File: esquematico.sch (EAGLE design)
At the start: 15 parts, among them IC1 TS321IDBVR, IC2 ESP32-S3-WROOM-1-N16R8, IC3 MAX30102EFD+T

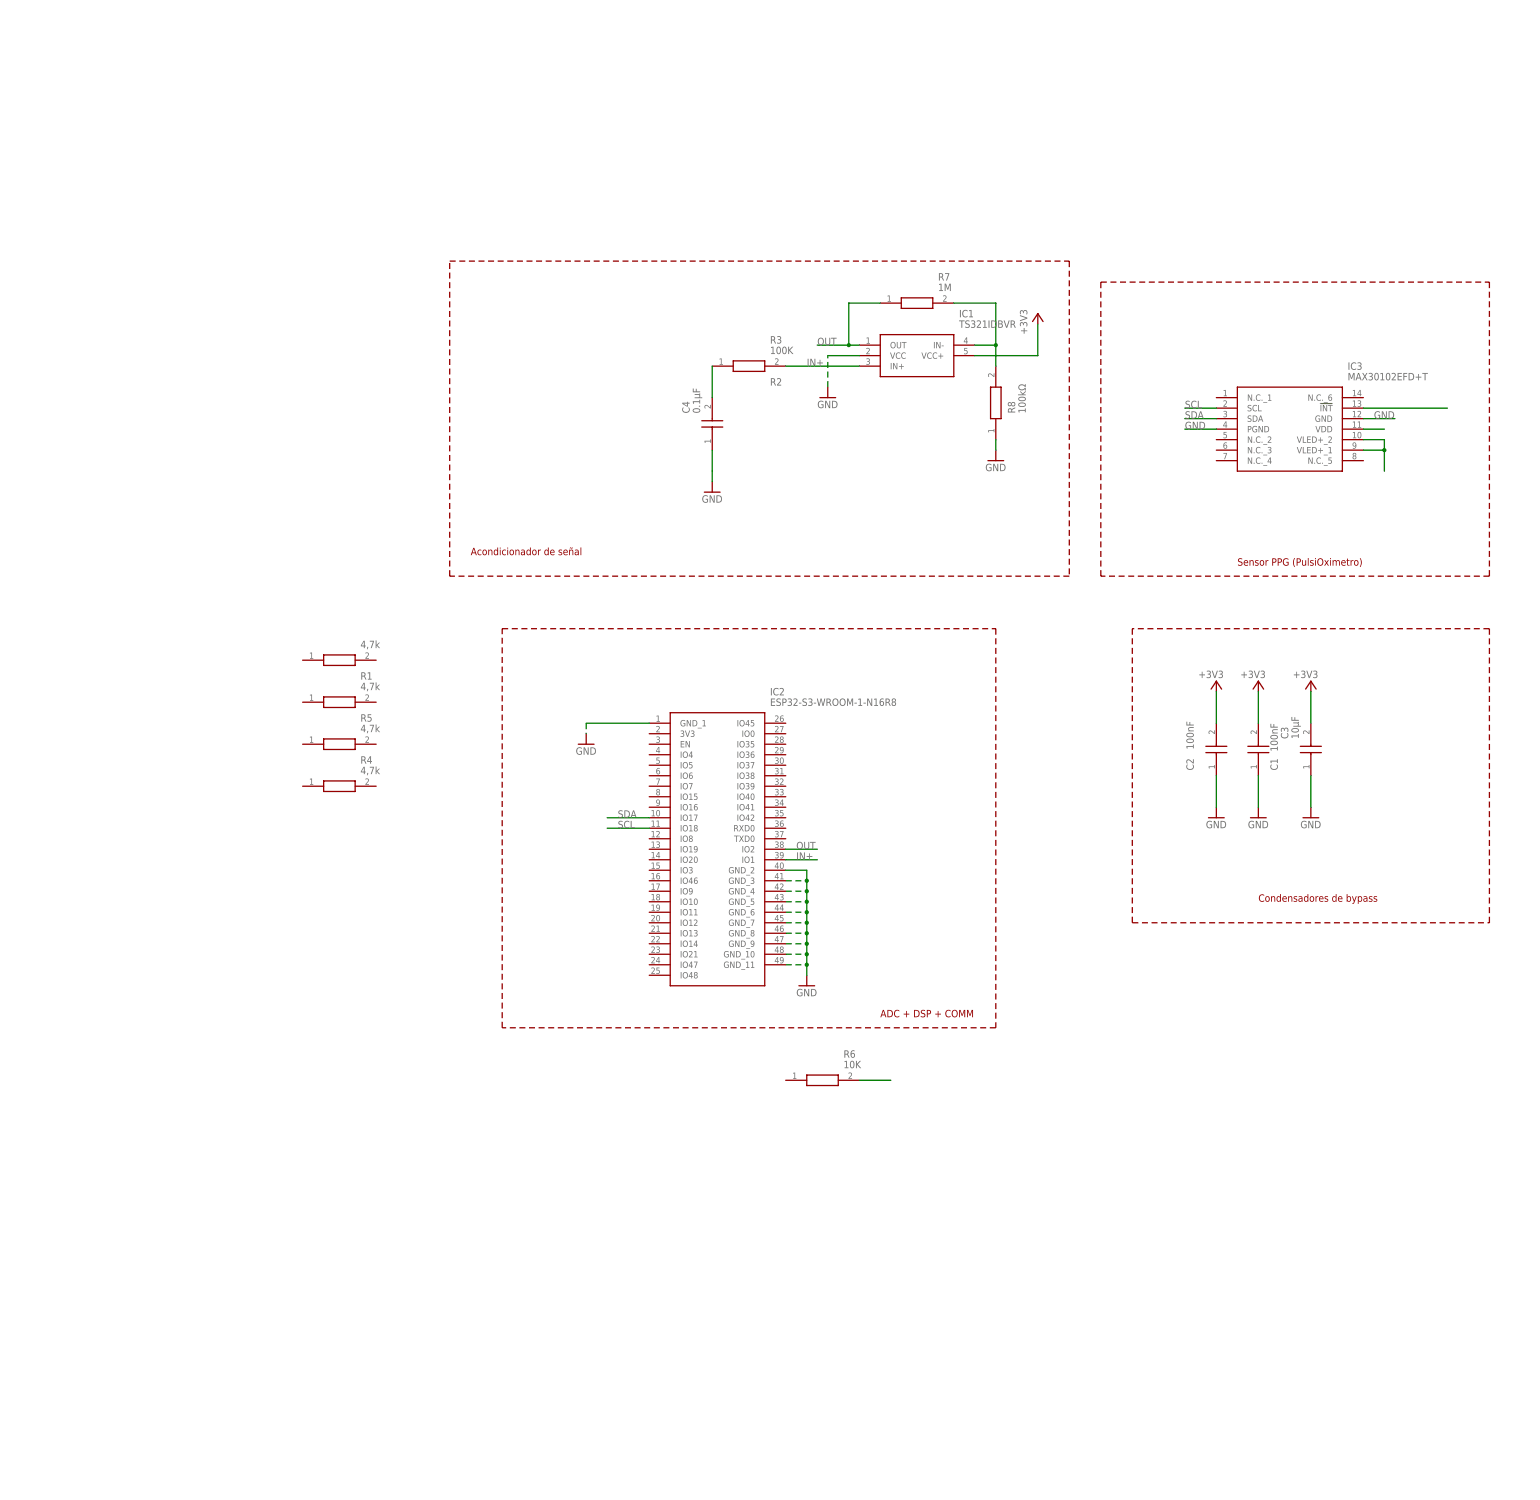
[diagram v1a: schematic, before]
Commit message: Finalizado bloque 2: Sensor PPG (PulsiOximetro)
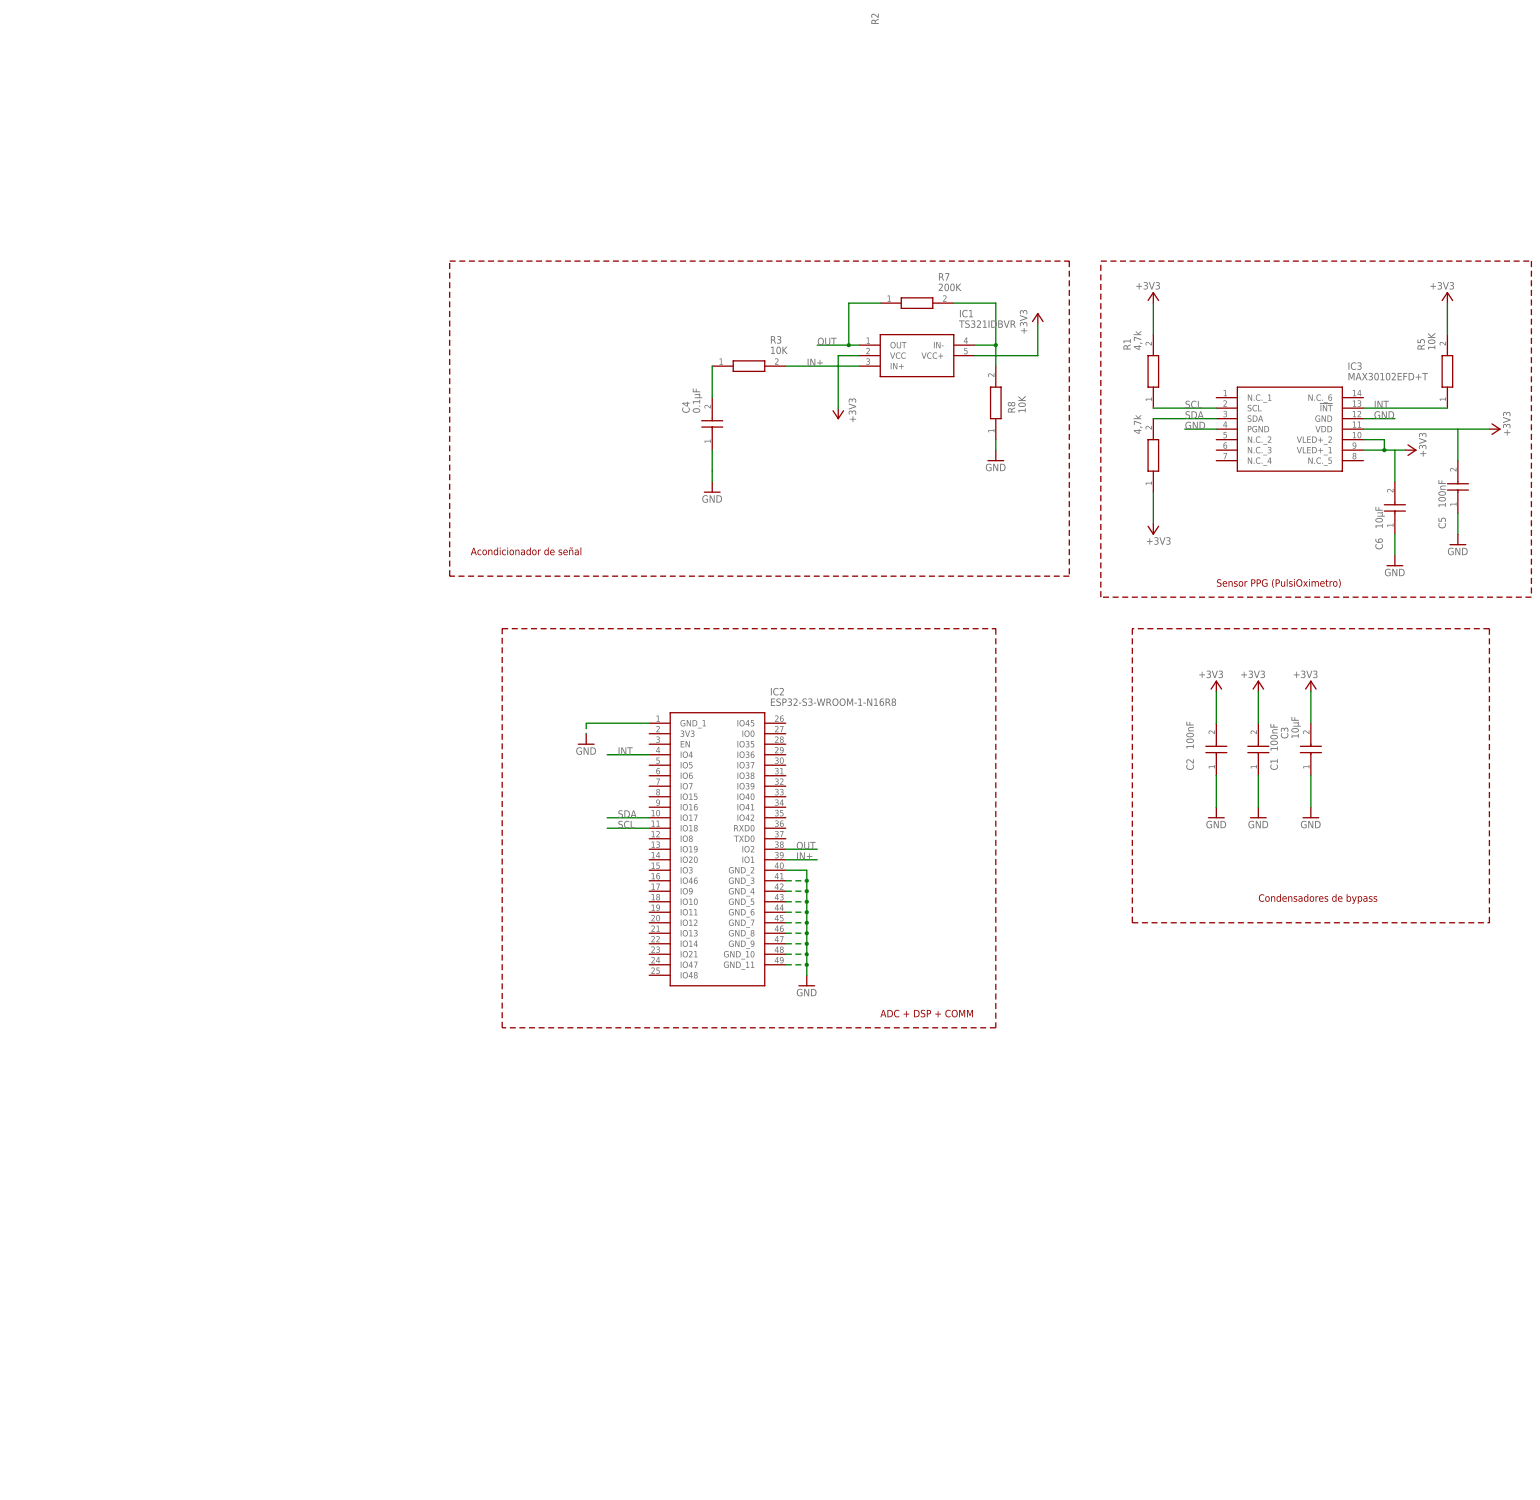
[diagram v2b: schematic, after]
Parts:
- removed R4: 4,7k, 0805S8F1202P5E:0805S8F1202P5E
- removed R6: 10K, 0805S8F1202P5E:0805S8F1202P5E
- added C5: 100nF, C0805J104K1RACAUTO:C0805J104K1RACAUTO
- added C6: 10µF, C0805J104K1RACAUTO:C0805J104K1RACAUTO
- R3: value 100K -> 10K
- R5: value 4,7k -> 10K
- R7: value 1M -> 200K
- R8: value 100kΩ -> 10K
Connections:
- removed net N$10: IC3.VDD
- removed net N$13: R6.2
- removed net N$15: IC3.!INT
- removed net N$16: IC3.VLED+_1, IC3.VLED+_2
- new net +3V1: C5.2
- new net +3V2: C6.2
- new net INT: IC2.IO4, IC3.!INT, R5.1
- net +3V3: now also IC1.VCC, IC3.VDD, IC3.VLED+_1, IC3.VLED+_2, R1.2, R2.1, R5.2
- net GND: now also C5.1, C6.1; no longer IC1.VCC
- net SCL: now also R1.1
- net SDA: now also R2.2
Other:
- moved on the sheet: R1, R2, R5

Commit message: Se corrigieron algunos bloques y se anoto lo faltante
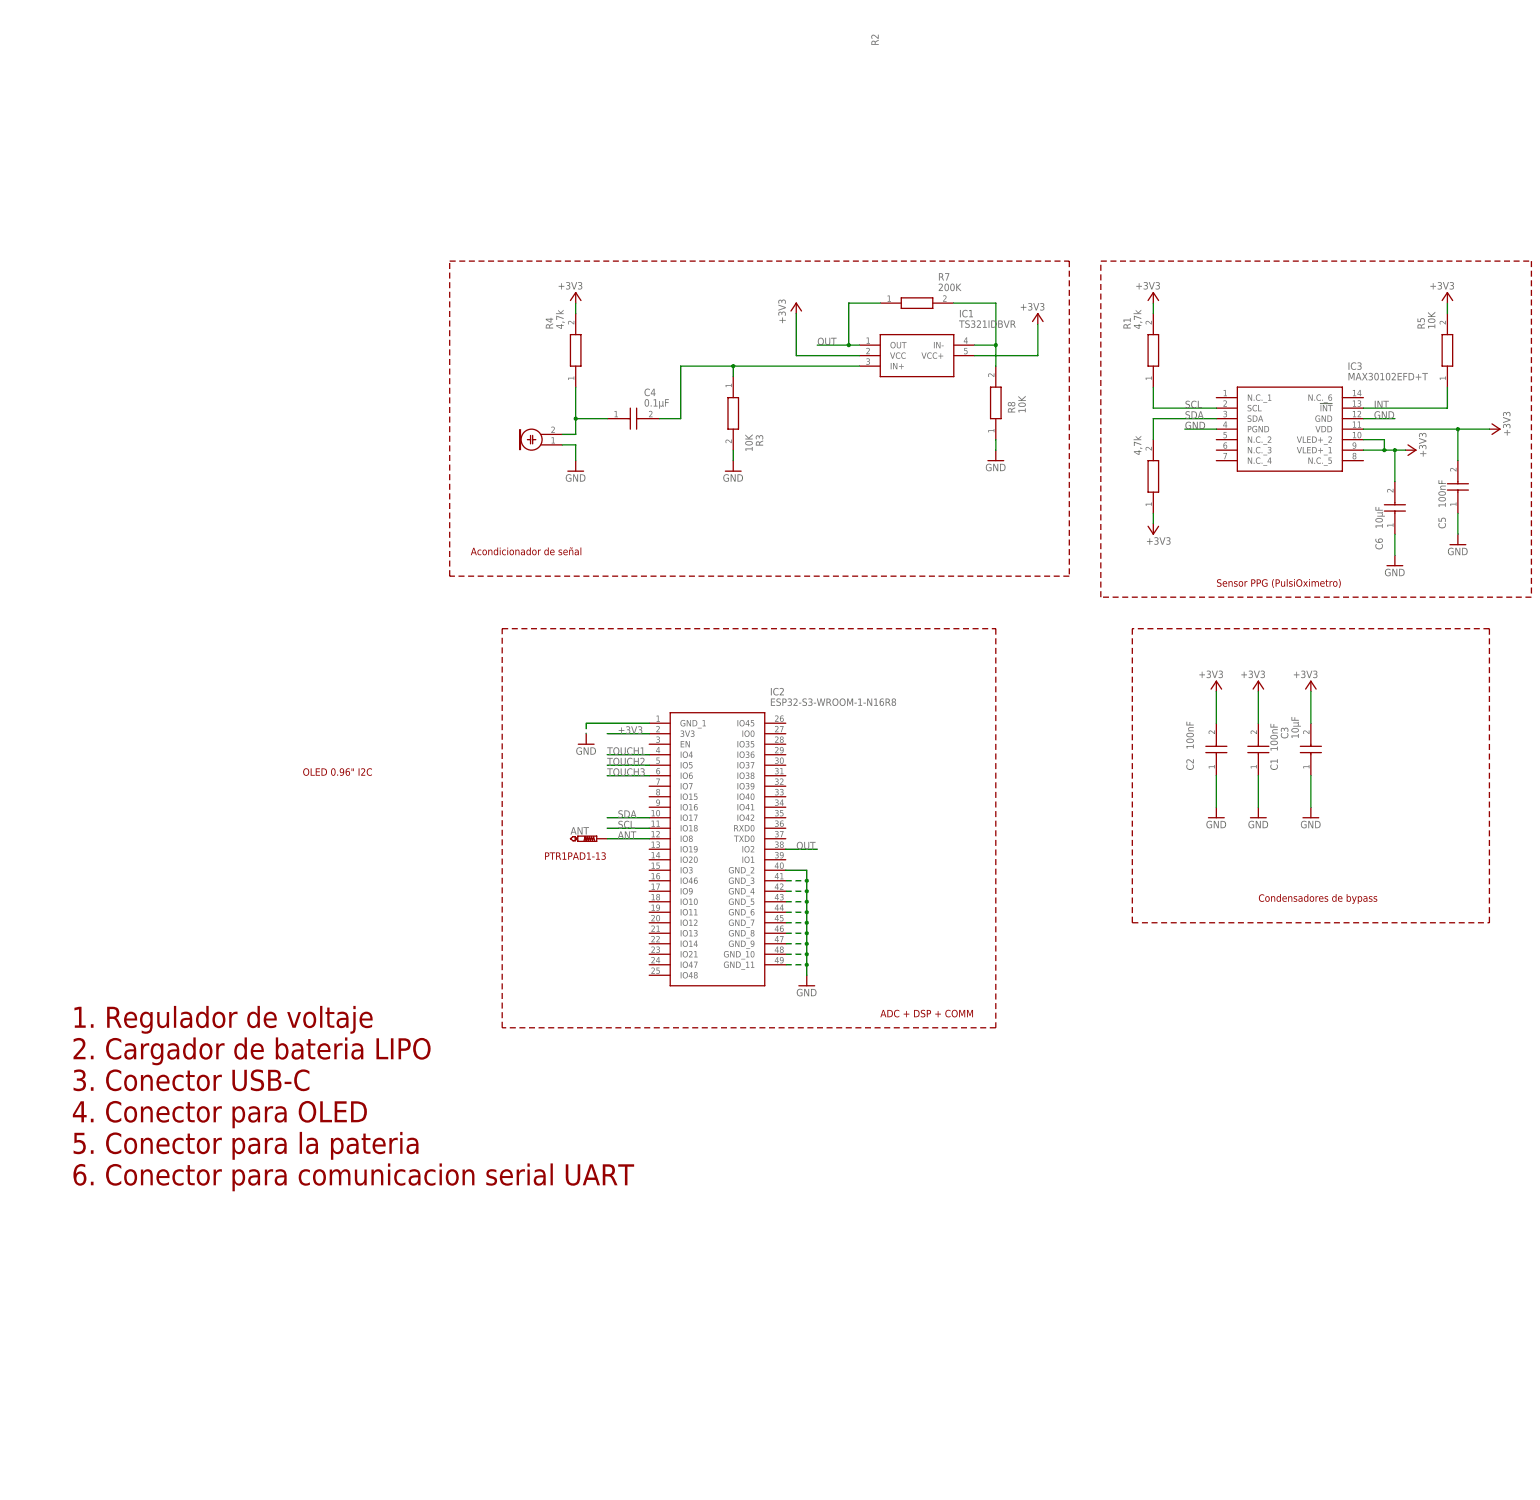
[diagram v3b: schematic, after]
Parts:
- added ANT: PTR1PAD1-13, testpad:PTR1PAD1-13
- added M1: ELECTRET_MICROPHON-WM.64PN, microphon:ELECTRET_MICROPHON-WM.64PN
- added R4: 4,7k, 0805S8F1202P5E:0805S8F1202P5E
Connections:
- removed net +3V1: C5.2
- removed net +3V2: C6.2
- removed net IN+: IC1.IN+, IC2.IO1, R3.2
- new net ANT: ANT.TP, IC2.IO8
- new net TOUCH1: IC2.IO4
- new net TOUCH2: IC2.IO5
- new net TOUCH3: IC2.IO6
- net +3V3: now also C5.2, C6.2, IC2.3V3, R4.2
- net GND: now also M1.1, R3.2
- net INT: no longer IC2.IO4
- net N$1: now also IC1.IN+
- net N$2: now also M1.2, R4.1
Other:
- note added: "1. Regulador de voltaje 2. Cargador de bateria LIPO 3. Conector USB-C 4. Conector para OLED 5. Conector para la pateria 6. Conector para comunicacion serial UART"
- note added: "OLED 0.96" I2C"
- note added: "PTR1PAD1-13"
- moved on the sheet: C4, R1, R2, R3, R5

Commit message: Add files via upload
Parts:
- added CN1: (no value), adafruit:USBMINIB
- added IC4: RV-3029-C2, crystal:RV-3029-C2
- added IC5: CP2101, silabs:CP2101
- added U1: LP38692SD-3.3/NOPB, LDO:LP38692SD-3.3/NOPB
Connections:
- new net POWER: U1.EN, U1.IN
- new net SC: IC4.SCL
- new net SD: IC4.SDA
- net +3V3: now also IC4.VDD, IC5.VBUS, U1.OUT
- net GND: now also IC4.VSS, IC5.GND, U1.GND
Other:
- note added: "REGULADOR DE VOLTAGE"
- moved on the sheet: ANT, IC2

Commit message: Add files via upload
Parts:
- removed IC5: CP2101, silabs:CP2101
- added B1: BATTERY_BR1225/FA, 52101-101-REV-A_v16:BATTERY_BR1225/FA
- added C7: 10µF, C0805J104K1RACAUTO:C0805J104K1RACAUTO
- added C8: 10µ, C0805J104K1RACAUTO:C0805J104K1RACAUTO
- added D1: (no value), 52101-101-REV-A_v16:LED_LEDCHIP-LED0603MP
- added K1: G6RW, relay:G6RW
- added R6: 220, 0805S8F1202P5E:0805S8F1202P5E
- added R9: 2k, 0805S8F1202P5E:0805S8F1202P5E
- added U2: MCP73831T-2ACI/OT, MCP73831:MCP73831T-2ACI/OT
- added U3: (no value), adafruit:GPS_FGPMMOPA6B
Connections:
- new net +BATT: U2.VBAT
- new net BATT: K12.S
- new net N$3: D1.C, R6.2
- new net N$5: R6.1, U2.STAT
- new net N$6: R9.2, U2.PROG
- new net N$7: B1.+, C8.2
- new net RX: U3.RX
- new net TX: U3.TX
- net +3V3: now also C7.2, CN1.VBUS, D1.A, K12.O, U2.VDD, U3.VCC; no longer IC5.VBUS
- net GND: now also B1.-, C7.1, C8.1, CN1.GND, R9.1, U2.VSS, U3.GND@2; no longer IC5.GND
- net POWER: now also K12.P
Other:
- note added: "ALIMENTACION"
- note added: "Conector para comunicacion serial UART"
- note removed: "1. Regulador de voltaje 2. Cargador de bateria LIPO 3. Conector USB-C 4. Conector para OLED 5. Conector para la pateria 6. Conector para comunicacion serial UART"
- moved on the sheet: ANT, C4, CN1, IC1, IC2, IC4, R3, R4, R7, R8

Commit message: Add files via upload
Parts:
- removed CN1: (no value), adafruit:USBMINIB
- removed IC4: RV-3029-C2, crystal:RV-3029-C2
- added SV1: (no value), con-lstb:MA04-1
- added U4: USB4115-03-C, usb:USB4115-03-C
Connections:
- removed net +3V3: C1.2, C2.2, C3.2, C5.2, C6.2, C7.2, CN1.VBUS, D1.A, IC1.VCC, IC1.VCC+, IC2.3V3, IC3.VDD, IC3.VLED+_1, IC3.VLED+_2, IC4.VDD, K12.O, R1.2, R2.1, R4.2, R5.2, U1.OUT, U2.VDD, U3.VCC
- removed net SC: IC4.SCL
- removed net SD: IC4.SDA
- new net D+: U4.DP2
- new net D+.: U4.DP1
- new net D-: U4.DN1
- new net D-.: U4.DN2
- new net N$9: SV1.2
- new net SDA.: SV1.4
- new net VBUS: C1.2, C2.2, C3.2, C5.2, C6.2, C7.2, D1.A, IC1.VCC, IC1.VCC+, IC2.3V3, IC3.VDD, IC3.VLED+_1, IC3.VLED+_2, K12.O, R1.2, R2.1, R4.2, R5.2, U1.OUT, U2.VDD, U3.VCC, U4.VBUS, U4.VBUS_2, U4.VBUS_3, U4.VBUS_4
- net GND: now also SV1.1, U4.GND_2, U4.GND_3, U4.GND_4, U4.GND_5; no longer CN1.GND, IC4.VSS
- net SCL: now also SV1.3
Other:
- moved on the sheet: B1, C7, C8, D1, R6, R9, U2
